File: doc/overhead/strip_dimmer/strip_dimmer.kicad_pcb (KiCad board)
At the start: 2 copper layers, 41 x 20 mm, 9 parts, among them J1 SERIAL_OUT, J2 POWER_IN, J4 POWER_OUT, J5 LED_STRIP, J6 SERIAL_IN, Q1 IRLB8721PBF, Q2 IRLB8721PBF, U1 ATtiny85-20S, U2 TPS70933DBVR

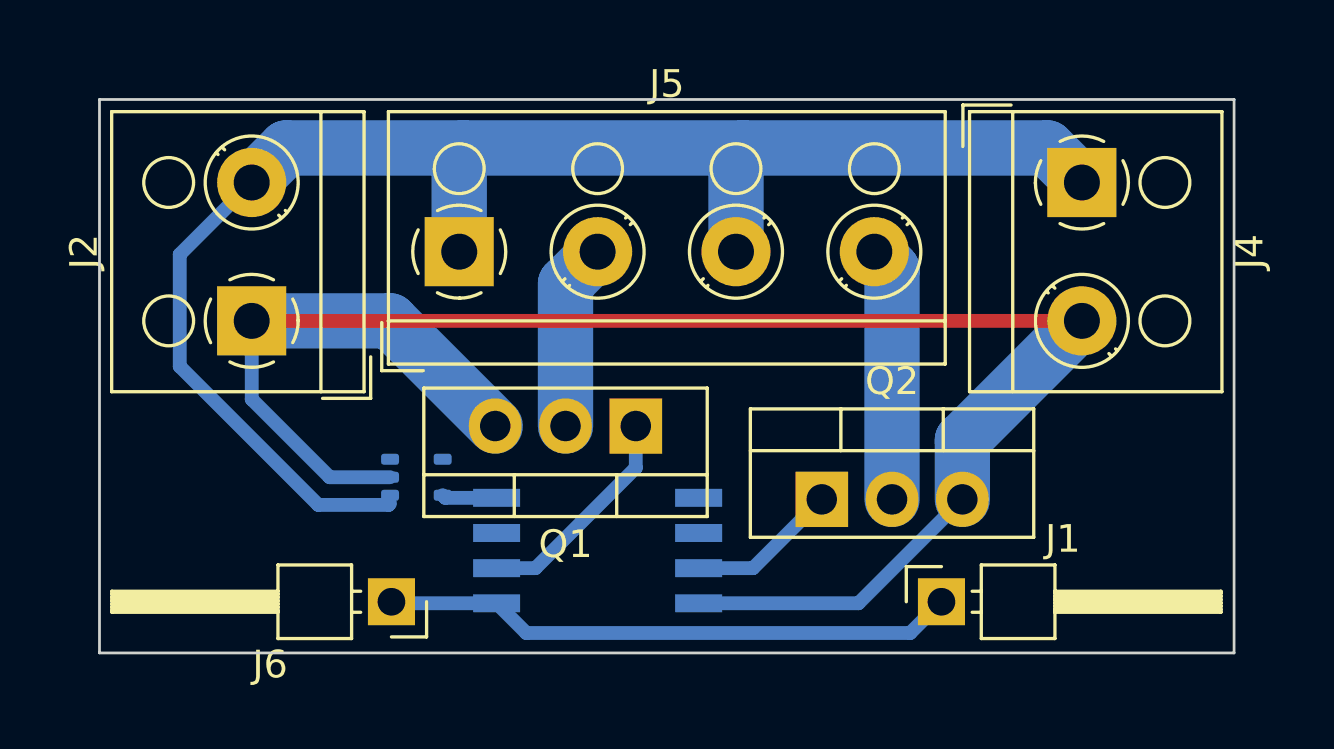
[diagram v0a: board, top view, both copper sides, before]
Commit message: Add PCB CAM and Voron toolboard stuff.
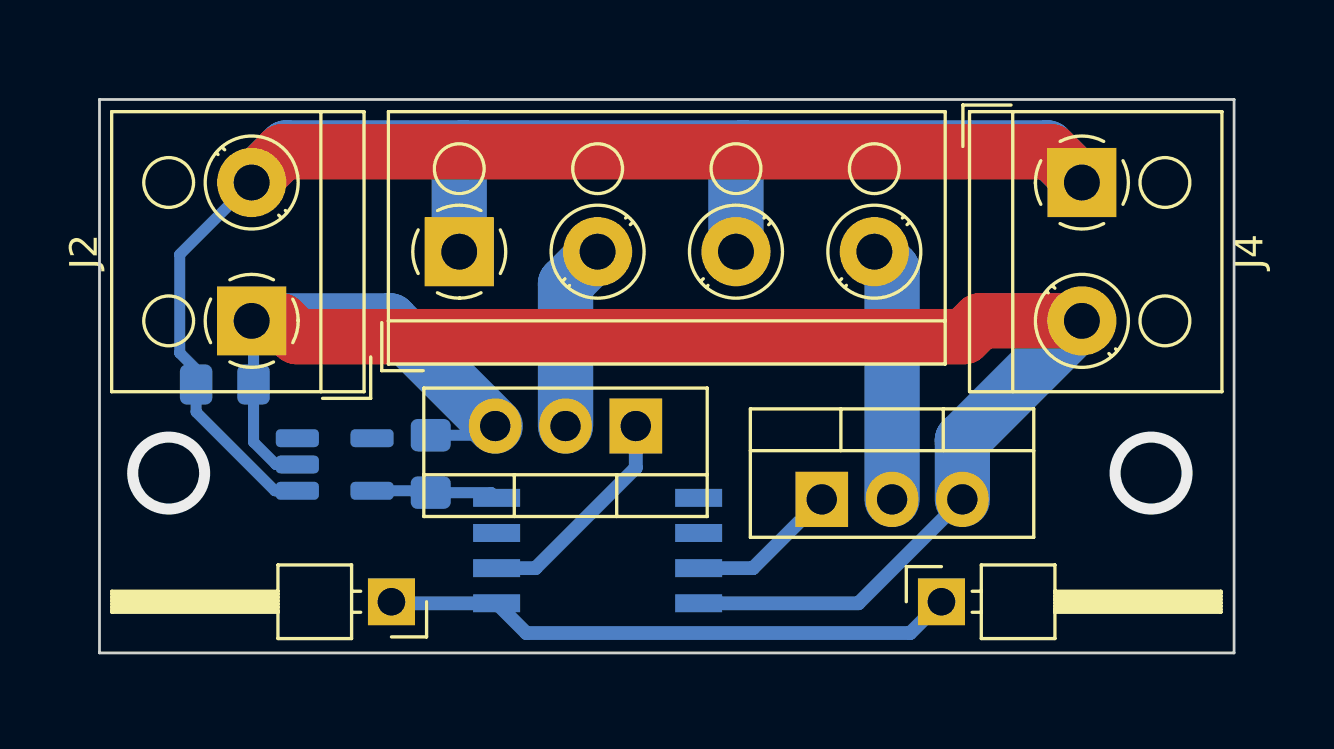
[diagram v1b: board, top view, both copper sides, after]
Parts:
- added C1: 2.2uF, Capacitor_SMD:C_0805_2012Metric_Pad1.18x1.45mm_HandSolder, B.Cu at (112.0, 113.2)
- added C2: 1uF, Capacitor_SMD:C_0805_2012Metric_Pad1.18x1.45mm_HandSolder, B.Cu at (104.5, 110.3)
- U2: footprint Package_TO_SOT_SMD:SOT-353_SC-70-5 -> Package_TO_SOT_SMD:SOT-23-5_HandSoldering
- moved U2 2.99 mm to (108.5, 113.2)
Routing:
- net +24V: track 56.1 -> 84.1 mm
- net +3V3: track 2.12 -> 4.61 mm
- net GND: track 69.1 -> 70.5 mm
- net (no net): vias 0 -> 2
